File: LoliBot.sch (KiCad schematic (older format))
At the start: 40 parts, among them J1 LOLINBATT, J10 LEFT-MOTOR, J11 REFLECT_, J12 MECH, J13 MECH, J14 MECH, J15 MECH, J16 MECH, J17 MECH, J18 MECH, J19 MECH, J2 APA106, J20 CONN_01X08, J21 CONN_01X06, J22 BRIDGE, J23 BRIDGE, J24 FUSE_BRIDGE, J25 MECH, J26 MECH, J27 MECH, J28 MECH, J29 MECH, J3 SERVO1, J30 MECH, J4 RIGHT, J5 LEFT, J6 MPU-9250, J7 APA106, J8 APA106, J9 RIGHT-MOTOR, SW1 SPST, U1 LOLIN32-LITE, U3 L9110, U4 L9110

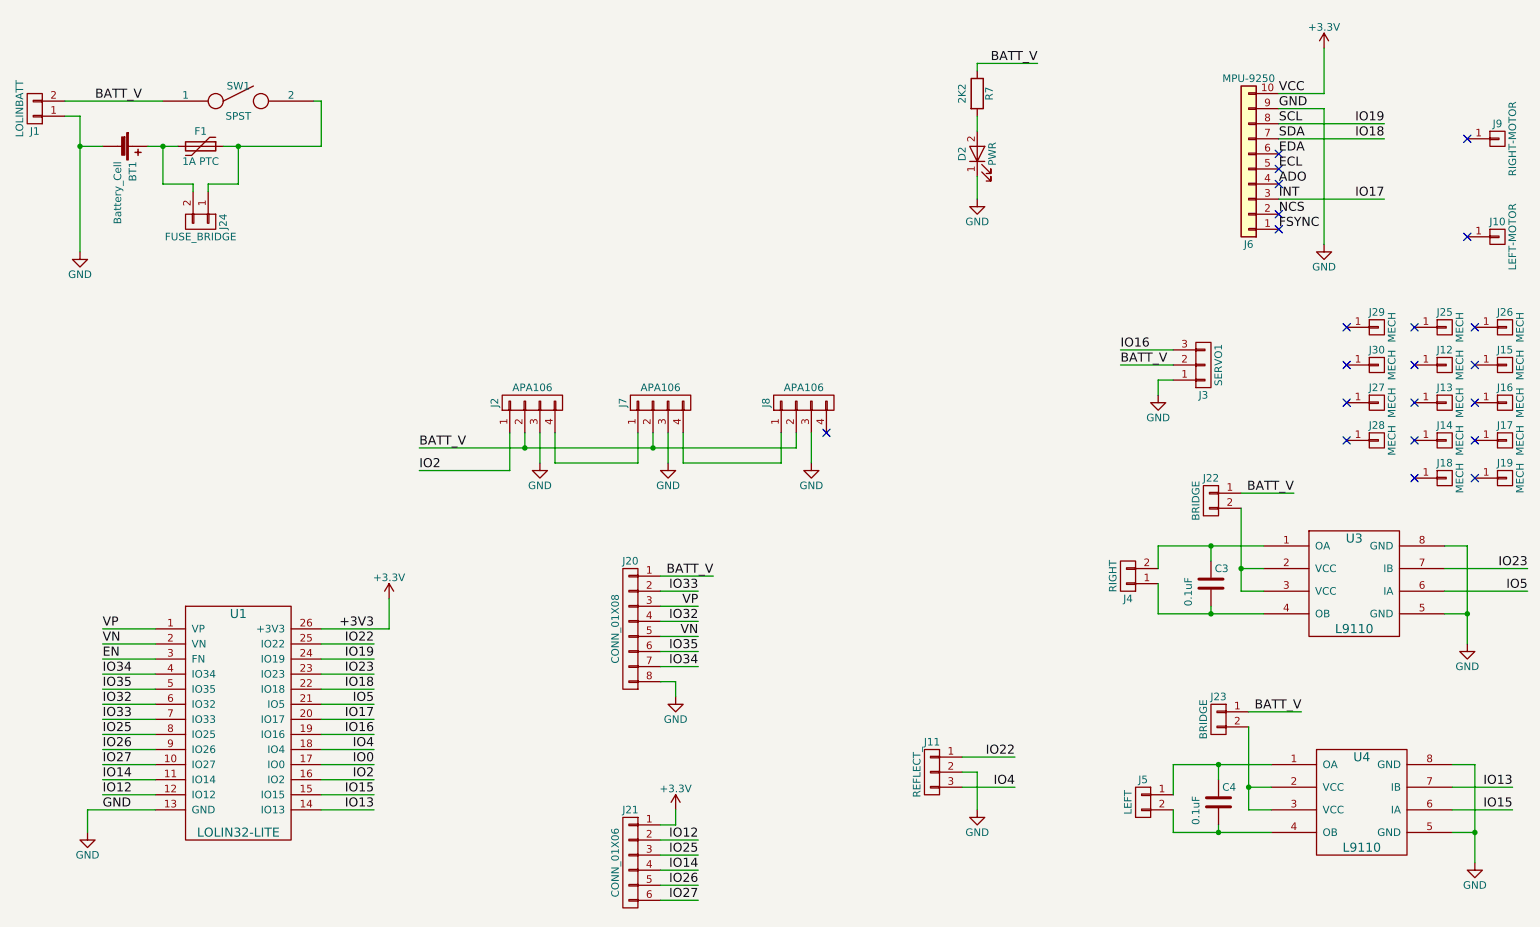
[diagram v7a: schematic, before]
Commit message: Added logos and text
And vias.
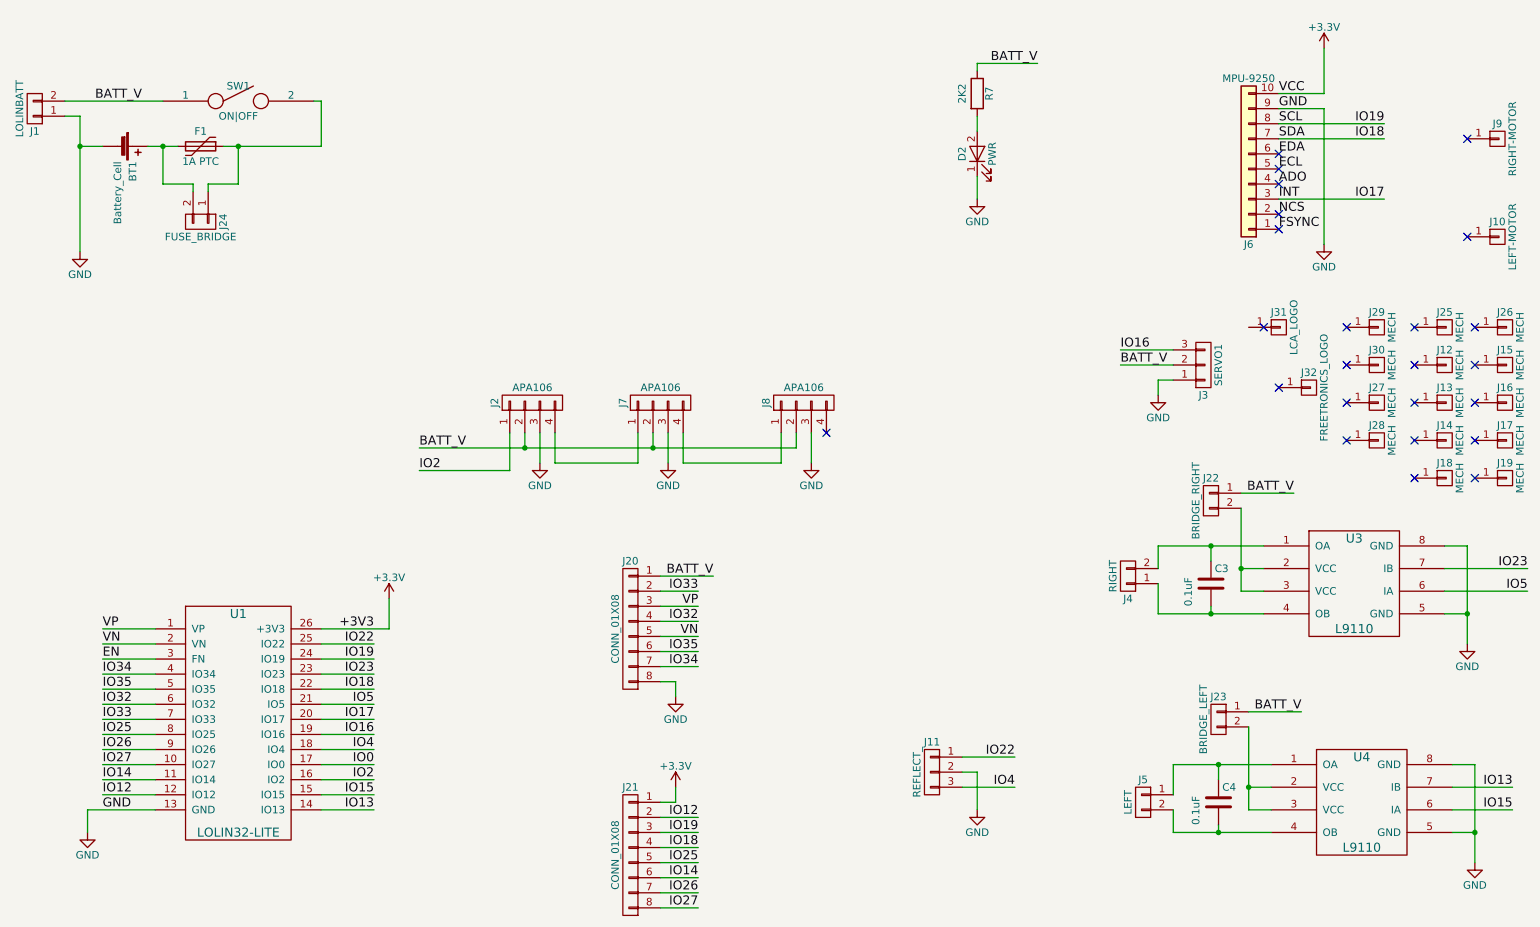
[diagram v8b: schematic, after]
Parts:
- removed J21: CONN_01X06, Pin_Headers:Pin_Header_Straight_2x03_Pitch2.54mm, symbol CONN_01X06
- added J21: CONN_01X08, Pin_Headers:Pin_Header_Straight_2x04_Pitch2.54mm, symbol CONN_01X08
- added J31: LCA_LOGO, libs:LCA2018_LOGO, symbol CONN_01X01
- added J32: FREETRONICS_LOGO, libs:LOGO_FREETRONICS_33mm, symbol CONN_01X01
- C3, C4: footprint Capacitors_SMD:C_0805_HandSoldering -> Capacitors_SMD:C_0603_HandSoldering
- J22: value BRIDGE -> BRIDGE_RIGHT
- J23: value BRIDGE -> BRIDGE_LEFT
- R7: footprint Resistors_SMD:R_0805_HandSoldering -> Resistors_SMD:R_0603_HandSoldering
- SW1: value SPST -> ON|OFF
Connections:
- net +3V3: now also J21.1 (P1)
- net IO12: now also J21.2 (P2)
- net IO14: now also J21.6 (P6)
- net IO18: now also J21.4 (P4)
- net IO19: now also J21.3 (P3)
- net IO25: now also J21.5 (P5)
- net IO26: now also J21.7 (P7)
- net IO27: now also J21.8 (P8)
- no-connect marks 22 -> 24
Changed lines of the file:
@@
 $EndComp
 $Comp
-L GND #PWR1
+L GND #PWR01
 U 1 1 59DB6136
 P 1250 2150
-F 0 "#PWR1" H 1250 1900 50  0001 C CNN
+F 0 "#PWR01" H 1250 1900 50  0001 C CNN
 F 1 "GND" H 1250 2000 50  0000 C CNN
 F 2 "" H 1250 2150 50  0001 C CNN
@@
 P 2300 1150
 F 0 "SW1" H 2300 1250 50  0000 C CNN
-F 1 "SPST" H 2300 1050 50  0000 C CNN
+F 1 "ON|OFF" H 2300 1050 50  0000 C CNN
 F 2 "libs:SS12D00" H 2300 1150 50  0001 C CNN
 F 3 "" H 2300 1150 50  0000 C CNN
@@
 $EndComp
 $Comp
-L GND #PWR9
+L GND #PWR02
 U 1 1 59DB834E
 P 7200 1800
-F 0 "#PWR9" H 7200 1550 50  0001 C CNN
+F 0 "#PWR02" H 7200 1550 50  0001 C CNN
 F 1 "GND" H 7200 1650 50  0000 C CNN
 F 2 "" H 7200 1800 50  0001 C CNN
@@
 F 0 "R7" V 7280 1100 50  0000 C CNN
 F 1 "2K2" V 7100 1100 50  0000 C CNN
-F 2 "Resistors_SMD:R_0805_HandSoldering" V 7130 1100 50  0001 C CNN
+F 2 "Resistors_SMD:R_0603_HandSoldering" V 7130 1100 50  0001 C CNN
 F 3 "" H 7200 1100 50  0001 C CNN
 	1    7200 1100
@@
 $EndComp
 $Comp
-L GND #PWR4
+L GND #PWR03
 U 1 1 59DBA675
 P 4300 3550
-F 0 "#PWR4" H 4300 3300 50  0001 C CNN
+F 0 "#PWR03" H 4300 3300 50  0001 C CNN
 F 1 "GND" H 4300 3400 50  0000 C CNN
 F 2 "" H 4300 3550 50  0001 C CNN
@@
 $EndComp
 $Comp
-L GND #PWR14
+L GND #PWR04
 U 1 1 59DBB61B
 P 10450 4750
-F 0 "#PWR14" H 10450 4500 50  0001 C CNN
+F 0 "#PWR04" H 10450 4500 50  0001 C CNN
 F 1 "GND" H 10450 4600 50  0000 C CNN
 F 2 "" H 10450 4750 50  0001 C CNN
@@
 $EndComp
 $Comp
-L GND #PWR15
+L GND #PWR05
 U 1 1 59DBCDC3
 P 10500 6200
-F 0 "#PWR15" H 10500 5950 50  0001 C CNN
+F 0 "#PWR05" H 10500 5950 50  0001 C CNN
 F 1 "GND" H 10500 6050 50  0000 C CNN
 F 2 "" H 10500 6200 50  0001 C CNN
@@
 $EndComp
 $Comp
-L GND #PWR11
+L GND #PWR06
 U 1 1 59DBDB38
 P 8400 3100
-F 0 "#PWR11" H 8400 2850 50  0001 C CNN
+F 0 "#PWR06" H 8400 2850 50  0001 C CNN
 F 1 "GND" H 8400 2950 50  0000 C CNN
 F 2 "" H 8400 3100 50  0001 C CNN
@@
 IO13
 $Comp
-L +3.3V #PWR3
+L +3.3V #PWR07
 U 1 1 59DC0699
 P 3300 4450
-F 0 "#PWR3" H 3300 4300 50  0001 C CNN
+F 0 "#PWR07" H 3300 4300 50  0001 C CNN
 F 1 "+3.3V" H 3300 4590 50  0000 C CNN
 F 2 "" H 3300 4450 50  0001 C CNN
@@
 $EndComp
 $Comp
-L GND #PWR2
+L GND #PWR08
 U 1 1 59DC0B2B
 P 1300 6000
-F 0 "#PWR2" H 1300 5750 50  0001 C CNN
+F 0 "#PWR08" H 1300 5750 50  0001 C CNN
 F 1 "GND" H 1300 5850 50  0000 C CNN
 F 2 "" H 1300 6000 50  0001 C CNN
@@
 FSYNC
 $Comp
-L +3.3V #PWR12
+L +3.3V #PWR09
 U 1 1 59E28F97
 P 9500 800
-F 0 "#PWR12" H 9500 650 50  0001 C CNN
+F 0 "#PWR09" H 9500 650 50  0001 C CNN
 F 1 "+3.3V" H 9500 940 50  0000 C CNN
 F 2 "" H 9500 800 50  0001 C CNN
@@
 	9500 1100 9500 800
 $Comp
-L GND #PWR13
+L GND #PWR010
 U 1 1 59E29073
 P 9500 2100
-F 0 "#PWR13" H 9500 1850 50  0001 C CNN
+F 0 "#PWR010" H 9500 1850 50  0001 C CNN
 F 1 "GND" H 9500 1950 50  0000 C CNN
 F 2 "" H 9500 2100 50  0001 C CNN
@@
 	5150 3350 5150 3550
 $Comp
-L GND #PWR5
+L GND #PWR011
 U 1 1 59E30F3C
 P 5150 3550
-F 0 "#PWR5" H 5150 3300 50  0001 C CNN
+F 0 "#PWR011" H 5150 3300 50  0001 C CNN
 F 1 "GND" H 5150 3400 50  0000 C CNN
 F 2 "" H 5150 3550 50  0001 C CNN
@@
 	6100 3350 6100 3550
 $Comp
-L GND #PWR8
+L GND #PWR012
 U 1 1 59F090C3
 P 6100 3550
-F 0 "#PWR8" H 6100 3300 50  0001 C CNN
+F 0 "#PWR012" H 6100 3300 50  0001 C CNN
 F 1 "GND" H 6100 3400 50  0000 C CNN
 F 2 "" H 6100 3550 50  0001 C CNN
@@
 $EndComp
 $Comp
-L GND #PWR10
+L GND #PWR013
 U 1 1 59F9DB04
 P 7200 5850
-F 0 "#PWR10" H 7200 5600 50  0001 C CNN
+F 0 "#PWR013" H 7200 5600 50  0001 C CNN
 F 1 "GND" H 7200 5700 50  0000 C CNN
 F 2 "" H 7200 5850 50  0001 C CNN
@@
 F 0 "C3" H 8775 4450 50  0000 L CNN
 F 1 "0.1uF" V 8600 4200 50  0000 L CNN
-F 2 "Capacitors_SMD:C_0805_HandSoldering" H 8788 4200 50  0001 C CNN
+F 2 "Capacitors_SMD:C_0603_HandSoldering" H 8788 4200 50  0001 C CNN
 F 3 "" H 8750 4350 50  0001 C CNN
 	1    8750 4350
@@
 F 0 "C4" H 8825 5900 50  0000 L CNN
 F 1 "0.1uF" V 8650 5650 50  0000 L CNN
-F 2 "Capacitors_SMD:C_0805_HandSoldering" H 8838 5650 50  0001 C CNN
+F 2 "Capacitors_SMD:C_0603_HandSoldering" H 8838 5650 50  0001 C CNN
 F 3 "" H 8800 5800 50  0001 C CNN
 	1    8800 5800
@@
 $EndComp
 $Comp
-L +3.3V #PWR7
+L +3.3V #PWR014
 U 1 1 5A117D1F
-P 5200 5850
-F 0 "#PWR7" H 5200 5700 50  0001 C CNN
-F 1 "+3.3V" H 5200 5990 50  0000 C CNN
-F 2 "" H 5200 5850 50  0001 C CNN
-F 3 "" H 5200 5850 50  0001 C CNN
-	1    5200 5850
+P 5200 5700
+F 0 "#PWR014" H 5200 5550 50  0001 C CNN
+F 1 "+3.3V" H 5200 5840 50  0000 C CNN
+F 2 "" H 5200 5700 50  0001 C CNN
+F 3 "" H 5200 5700 50  0001 C CNN
+	1    5200 5700
 	1    0    0    -1
 $EndComp
@@
 IO33
 $Comp
-L GND #PWR6
+L GND #PWR015
 U 1 1 5A1181BF
 P 5200 5100
-F 0 "#PWR6" H 5200 4850 50  0001 C CNN
+F 0 "#PWR015" H 5200 4850 50  0001 C CNN
 F 1 "GND" H 5200 4950 50  0000 C CNN
 F 2 "" H 5200 5100 50  0001 C CNN
@@
 Wire Wire Line
 	5350 4900 5100 4900
-Text Label 5350 6150 2    60   ~ 0
+Text Label 5350 6200 2    60   ~ 0
 IO25
-Text Label 5350 6350 2    60   ~ 0
+Text Label 5350 6400 2    60   ~ 0
 IO26
-Text Label 5350 6450 2    60   ~ 0
+Text Label 5350 6500 2    60   ~ 0
 IO27
-Text Label 5350 6250 2    60   ~ 0
+Text Label 5350 6300 2    60   ~ 0
 IO14
-Text Label 5350 6050 2    60   ~ 0
+Text Label 5350 5900 2    60   ~ 0
 IO12
-$Comp
-L CONN_01X06 J21
-U 1 1 5A11A25A
-P 4900 6200
-F 0 "J21" H 4900 6550 50  0000 C CNN
-F 1 "CONN_01X06" V 5000 6200 50  0000 C CNN
-F 2 "Pin_Headers:Pin_Header_Straight_2x03_Pitch2.54mm" H 4900 6200 50  0001 C CNN
-F 3 "" H 4900 6200 50  0001 C CNN
-	1    4900 6200
-	-1   0    0    -1
-$EndComp
-Wire Wire Line
-	5100 5950 5200 5950
-Wire Wire Line
-	5200 5950 5200 5850
-Wire Wire Line
-	5100 6050 5350 6050
-Wire Wire Line
-	5350 6150 5100 6150
-Wire Wire Line
-	5100 6250 5350 6250
-Wire Wire Line
-	5350 6350 5100 6350
-Wire Wire Line
-	5100 6450 5350 6450
+Wire Wire Line
+	5100 5800 5200 5800
+Wire Wire Line
+	5200 5800 5200 5700
+Wire Wire Line
+	5100 5900 5350 5900
+Wire Wire Line
+	5350 6200 5100 6200
+Wire Wire Line
+	5100 6300 5350 6300
+Wire Wire Line
+	5350 6400 5100 6400
+Wire Wire Line
+	5100 6500 5350 6500
 NoConn ~ 10500 2900
 NoConn ~ 10500 3150
@@
 P 8750 3800
 F 0 "J22" H 8750 3950 50  0000 C CNN
-F 1 "BRIDGE" V 8850 3800 50  0000 C CNN
+F 1 "BRIDGE_RIGHT" V 8850 3800 50  0000 C CNN
 F 2 "Pin_Headers:Pin_Header_Straight_1x02_Pitch2.54mm" H 8750 3800 50  0001 C CNN
 F 3 "" H 8750 3800 50  0001 C CNN
@@
 P 8800 5250
 F 0 "J23" H 8800 5400 50  0000 C CNN
-F 1 "BRIDGE" V 8900 5250 50  0000 C CNN
+F 1 "BRIDGE_LEFT" V 8900 5250 50  0000 C CNN
 F 2 "Pin_Headers:Pin_Header_Straight_1x02_Pitch2.54mm" H 8800 5250 50  0001 C CNN
 F 3 "" H 8800 5250 50  0001 C CNN
@@
 	2800 1150 2850 1150
 Wire Wire Line
-	2850 1150 2850 1450
+	2850 1450 2850 1150
 Text Label 1350 1150 0    60   ~ 0
 BATT_V
@@
 $EndComp
 Wire Wire Line
-	2850 1450 2200 1450
-Wire Wire Line
-	1900 1450 1700 1450
+	2200 1450 2850 1450
+Wire Wire Line
+	1700 1450 1900 1450
 $Comp
 L CONN_01X02 J24
@@
 NoConn ~ 9650 2650
 NoConn ~ 9650 2900
+$Comp
+L CONN_01X01 J31
+U 1 1 5A2E7715
+P 9200 2650
+F 0 "J31" H 9200 2750 50  0000 C CNN
+F 1 "LCA_LOGO" V 9300 2650 50  0000 C CNN
+F 2 "libs:LCA2018_LOGO" H 9200 2650 50  0001 C CNN
+F 3 "" H 9200 2650 50  0001 C CNN
+	1    9200 2650
+	1    0    0    -1
+$EndComp
+NoConn ~ 9100 2650
+$Comp
+L CONN_01X01 J32
+U 1 1 5A2E8892
+P 9400 3050
+F 0 "J32" H 9400 3150 50  0000 C CNN
+F 1 "FREETRONICS_LOGO" V 9500 3050 50  0000 C CNN
+F 2 "libs:LOGO_FREETRONICS_33mm" H 9400 3050 50  0001 C CNN
+F 3 "" H 9400 3050 50  0001 C CNN
+	1    9400 3050
+	1    0    0    -1
+$EndComp
+NoConn ~ 9200 3050
+$Comp
+L CONN_01X08 J21
+U 1 1 5A2EC05A
+P 4900 6150
+F 0 "J21" H 4900 6600 50  0000 C CNN
+F 1 "CONN_01X08" V 5000 6150 50  0000 C CNN
+F 2 "Pin_Headers:Pin_Header_Straight_2x04_Pitch2.54mm" H 4900 6150 50  0001 C CNN
+F 3 "" H 4900 6150 50  0001 C CNN
+	1    4900 6150
+	-1   0    0    -1
+$EndComp
+Wire Wire Line
+	5100 6000 5350 6000
+Wire Wire Line
+	5100 6100 5350 6100
+Text Label 5350 6000 2    60   ~ 0
+IO19
+Text Label 5350 6100 2    60   ~ 0
+IO18
 $EndSCHEMATC
